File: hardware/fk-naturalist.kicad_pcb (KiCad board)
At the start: 2 copper layers, 106 x 37 mm, 140 parts, among them J1 Conn_01x11, J10 S2B-PH-SM4-TB, J11 RF-SMA-EDGE, J2 Conn_01x05, J3 Conn_01x04, J5 Conn_01x03, J6 Conn_01x05, J7 CONN-HDR-2x5, J8 Conn_01x09, J9 MICRO-USB, M1 MOUNT_HOLE, M3 MOUNT_HOLE, M4 MOUNT_HOLE, M6 MOUNT_HOLE, M7 MICROSD, Q1 2N7002LT1G, Q2 2N7002LT1G, Q3 2N7002LT1G, Q4 2N7002LT1G, SW1 SPNO, SW2 SPNO, U1 ATWINC1500-MR210PA, U10 FGPMMOPA6H, U101 TSL2591, U102 MPL3115A2, U103 BNO055, U104 SHT31, U11 MAX1704XX, U2 ATSAMD21G18A-AU, U3 SPH0645, U4 24AA02E64, U5 S25FL116K0XMFI041, U6 BQ24074RGTT, U7 PCF8523, U8 MCP1700T-3302E/MB, U9 ISL8541x, Y1 FC-135, Y101 FC-135, Y2 FC-135

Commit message: More label/naming cleanup.
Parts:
- C10, C19, C20, C25: value 4.7uF 10V X5R -> 4.7uF
- C12: value 1uF 50V X5R -> 1uF
- C14: value 4.7nF 25V X7R -> 4.7nF
- C21, C23, C27, C29, C6: value 1uF 10V X5R -> 1uF
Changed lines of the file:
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@@
     (links 368)
     (no_connects 106)
-    (area 62.463333 99.838199 191.661515 152.064743)
+    (area 77.293399 109.703799 183.463001 146.887001)
     (thickness 1.6)
     (drawings 52)
@@
   )
   (layers
-    (0 F.Cu signal hide)
+    (0 F.Cu signal)
     (31 B.Cu signal)
     (32 B.Adhes user)
@@
     (46 B.CrtYd user)
     (47 F.CrtYd user)
-    (48 B.Fab user hide)
+    (48 B.Fab user)
     (49 F.Fab user)
   )
@@
       (effects (font (size 1 1) (thickness 0.15)))
     )
-    (fp_text value "1uF 10V X5R" (at 0.5969 0.1016 90) (layer F.Fab)
+    (fp_text value 1uF (at 0.5969 0.1016 90) (layer F.Fab)
       (effects (font (size 1 1) (thickness 0.15)))
     )
@@
       (effects (font (size 1 1) (thickness 0.15)))
     )
-    (fp_text value "4.7uF 10V X5R" (at 0.198714 0.095444) (layer F.Fab)
+    (fp_text value 4.7uF (at -3.369986 0.082744) (layer F.Fab)
       (effects (font (size 1 1) (thickness 0.15)))
     )
@@
       (effects (font (size 1 1) (thickness 0.15)))
     )
-    (fp_text value "1uF 50V X5R" (at -1.652953 -0.050941 180) (layer F.Fab)
+    (fp_text value 1uF (at -0.103553 1.384159 180) (layer F.Fab)
       (effects (font (size 1 1) (thickness 0.15)))
     )
@@
       (effects (font (size 1 1) (thickness 0.15)))
     )
-    (fp_text value "4.7nF 25V X7R" (at 7.235195 0.175542 90) (layer F.Fab)
+    (fp_text value 4.7nF (at 0.135895 1.534442 90) (layer F.Fab)
       (effects (font (size 1 1) (thickness 0.15)))
     )
@@
       (effects (font (size 1 1) (thickness 0.15)))
     )
-    (fp_text value "4.7uF 10V X5R" (at -2.4892 1.4478 180) (layer F.Fab)
+    (fp_text value 4.7uF (at -0.2159 1.4605 180) (layer F.Fab)
       (effects (font (size 1 1) (thickness 0.15)))
     )
@@
       (effects (font (size 1 1) (thickness 0.15)))
     )
-    (fp_text value "4.7uF 10V X5R" (at 2.085653 0.241441) (layer F.Fab)
+    (fp_text value 4.7uF (at -2.054547 0.038241) (layer F.Fab)
       (effects (font (size 1 1) (thickness 0.15)))
     )
@@
       (effects (font (size 1 1) (thickness 0.15)))
     )
-    (fp_text value "1uF 10V X5R" (at 0.713153 0.012841) (layer F.Fab)
+    (fp_text value 1uF (at -2.601547 -0.025259) (layer F.Fab)
       (effects (font (size 1 1) (thickness 0.15)))
     )
@@
       (effects (font (size 1 1) (thickness 0.15)))
     )
-    (fp_text value "4.7uF 10V X5R" (at -1.581277 -0.0254 270) (layer F.Fab)
+    (fp_text value 4.7uF (at 2.622423 -0.0635 270) (layer F.Fab)
       (effects (font (size 1 1) (thickness 0.15)))
     )
@@
       (effects (font (size 1 1) (thickness 0.15)))
     )
-    (fp_text value 100nF (at 3.371723 0.047919 270) (layer F.Fab)
+    (fp_text value 100nF (at 3.066923 -0.015581 270) (layer F.Fab)
       (effects (font (size 1 1) (thickness 0.15)))
     )
@@
       (effects (font (size 1 1) (thickness 0.15)))
     )
-    (fp_text value "1uF 10V X5R" (at 6.43231 0.026186) (layer F.Fab)
+    (fp_text value 1uF (at 2.83821 0.013486) (layer F.Fab)
       (effects (font (size 1 1) (thickness 0.15)))
     )
@@
       (effects (font (size 1 1) (thickness 0.15)))
     )
-    (fp_text value 10nF (at -3.21921 0.062714 180) (layer F.Fab)
+    (fp_text value 10nF (at -2.27941 0.989814 180) (layer F.Fab)
       (effects (font (size 1 1) (thickness 0.15)))
     )
@@
       (effects (font (size 1 1) (thickness 0.15)))
     )
-    (fp_text value "1uF 10V X5R" (at -3.5297 1.3589 270) (layer F.Fab)
+    (fp_text value 1uF (at -0.4563 1.3843 270) (layer F.Fab)
       (effects (font (size 1 1) (thickness 0.15)))
     )
@@
       (effects (font (size 1 1) (thickness 0.15)))
     )
-    (fp_text value 100pF (at 0 1.9 90) (layer F.Fab)
+    (fp_text value 100pF (at -0.889644 -1.312786 90) (layer F.Fab)
       (effects (font (size 1 1) (thickness 0.15)))
     )
@@
       (effects (font (size 1 1) (thickness 0.15)))
     )
-    (fp_text value Green (at -3.8862 1.1938 180) (layer F.Fab)
+    (fp_text value Green (at -0.1524 1.4732 180) (layer F.Fab)
       (effects (font (size 1 1) (thickness 0.15)))
     )
@@
       (effects (font (size 1 1) (thickness 0.15)))
     )
-    (fp_text value 24AA02E64 (at 6.584592 -0.101358 90) (layer F.Fab)
+    (fp_text value 24AA02E64 (at 6.038492 -0.126758 90) (layer F.Fab) hide
       (effects (font (size 1 1) (thickness 0.15)))
     )
-    (fp_text user %R (at 0 0 180) (layer F.Fab)
+    (fp_text user %R (at 0 0 180) (layer F.Fab) hide
       (effects (font (size 0.5 0.5) (thickness 0.075)))
     )
@@
       (effects (font (size 1 1) (thickness 0.15)))
     )
-    (fp_text value 1uF (at -2.569376 0.0889 90) (layer F.Fab)
+    (fp_text value 1uF (at 2.777324 -0.0127 90) (layer F.Fab)
       (effects (font (size 1 1) (thickness 0.15)))
     )
@@
       (effects (font (size 1 1) (thickness 0.15)))
     )
-    (fp_text value "1uF 10V X5R" (at -0.5461 0 180) (layer F.Fab)
+    (fp_text value 1uF (at -0.5461 0 180) (layer F.Fab)
       (effects (font (size 1 1) (thickness 0.15)))
     )

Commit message: Fix USB footprint with oval drills.
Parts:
- J9: footprint RocketScreamKicadLibrary:MICRO-USB -> conservify:MICRO-USB
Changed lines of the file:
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@@
   (general
     (links 368)
-    (no_connects 106)
+    (no_connects 0)
     (area 77.293399 109.703799 183.463001 146.887001)
     (thickness 1.6)
@@
       (net 2 3V3))
   )
-  (module RocketScreamKicadLibrary:MICRO-USB (layer F.Cu)
-    (at 80.9752 122.8344 270)
-    (tags MICRO-USB)
-    (fp_text reference J9 (at 0 -3.556 270) (layer F.SilkS) hide
-      (effects (font (size 1 1) (thickness 0.15)))
-    )
-    (fp_text value MICRO-USB (at 0 4.318 270) (layer F.Fab) hide
-      (effects (font (size 1 1) (thickness 0.15)))
-    )
-    (fp_line (start -4.55 -2.4) (end -4.55 3.45) (layer F.CrtYd) (width 0.05))
-    (fp_line (start -4.55 3.45) (end 4.55 3.45) (layer F.CrtYd) (width 0.05))
-    (fp_line (start 4.55 3.45) (end 4.55 -2.4) (layer F.CrtYd) (width 0.05))
-    (fp_line (start 4.55 -2.4) (end -4.55 -2.4) (layer F.CrtYd) (width 0.05))
-    (fp_circle (center -1.746 -2.608) (end -1.796 -2.658) (layer F.SilkS) (width 0.3))
-    (fp_line (start 3.8 0) (end 3.8 -1.55) (layer F.SilkS) (width 0.15))
-    (fp_line (start 3.8 -1.55) (end 3.25 -1.55) (layer F.SilkS) (width 0.15))
-    (fp_line (start -3.8 0) (end -3.8 -1.55) (layer F.SilkS) (width 0.15))
-    (fp_line (start -3.8 -1.55) (end -3.25 -1.55) (layer F.SilkS) (width 0.15))
-    (fp_line (start 3.8 2.2) (end 3.8 3.3) (layer F.SilkS) (width 0.15))
-    (fp_line (start -3.8 3.3) (end -3.8 2.2) (layer F.SilkS) (width 0.15))
-    (fp_line (start -3.8 3.3) (end 3.8 3.3) (layer F.SilkS) (width 0.15))
-    (pad 1 smd rect (at -1.3 -1.45 270) (size 0.4 1.35) (layers F.Cu F.Paste F.Mask)
-      (net 44 VUSB))
-    (pad 2 smd rect (at -0.65 -1.45 270) (size 0.4 1.35) (layers F.Cu F.Paste F.Mask)
-      (net 22 /USB-))
-    (pad 3 smd rect (at 0 -1.45 270) (size 0.4 1.35) (layers F.Cu F.Paste F.Mask)
-      (net 23 /USB+))
-    (pad 4 smd rect (at 0.65 -1.45 270) (size 0.4 1.35) (layers F.Cu F.Paste F.Mask)
-      (net 80 "Net-(J9-Pad4)"))
-    (pad 5 smd rect (at 1.3 -1.45 270) (size 0.4 1.35) (layers F.Cu F.Paste F.Mask)
-      (net 1 GND))
-    (pad 6 thru_hole circle (at -2.425 -1.525 270) (size 1.2 1.2) (drill 0.7) (layers *.Cu *.Mask F.SilkS)
-      (net 56 "Net-(C14-Pad1)"))
-    (pad 7 thru_hole circle (at 2.425 -1.525 270) (size 1.2 1.2) (drill 0.7) (layers *.Cu *.Mask F.SilkS)
-      (net 143 "Net-(J9-Pad7)"))
-    (pad 8 thru_hole oval (at -3.625 1.125 270) (size 1.3 1.7) (drill oval 0.7 1.1) (layers *.Cu *.Mask F.SilkS)
-      (net 81 "Net-(J9-Pad8)"))
-    (pad 9 thru_hole oval (at 3.625 1.125 270) (size 1.3 1.7) (drill oval 0.7 1.1) (layers *.Cu *.Mask F.SilkS)
-      (net 82 "Net-(J9-Pad9)"))
-  )
   (module RocketScreamKicadLibrary:S2B-PH-SM4-TB (layer F.Cu)
     (at 85.2452 141.726)
@@
     )
   )
+  (module conservify:MICRO-USB (layer F.Cu)
+    (at 80.9752 122.8344 270)
+    (tags MICRO-USB)
+    (fp_text reference J9 (at -26.162 0 270) (layer F.SilkS) hide
+      (effects (font (size 0.8 0.8) (thickness 0.15)))
+    )
+    (fp_text value MICRO-USB (at 0 4.318 270) (layer F.Fab) hide
+      (effects (font (size 0.8 0.8) (thickness 0.15)))
+    )
+    (fp_line (start -4.55 -2.4) (end -4.55 3.45) (layer F.CrtYd) (width 0.05))
+    (fp_line (start -4.55 3.45) (end 4.55 3.45) (layer F.CrtYd) (width 0.05))
+    (fp_line (start 4.55 3.45) (end 4.55 -2.4) (layer F.CrtYd) (width 0.05))
+    (fp_line (start 4.55 -2.4) (end -4.55 -2.4) (layer F.CrtYd) (width 0.05))
+    (fp_circle (center -1.746 -2.608) (end -1.796 -2.658) (layer F.SilkS) (width 0.3))
+    (fp_line (start 3.8 0) (end 3.8 -1.55) (layer F.SilkS) (width 0.15))
+    (fp_line (start 3.8 -1.55) (end 3.25 -1.55) (layer F.SilkS) (width 0.15))
+    (fp_line (start -3.8 0) (end -3.8 -1.55) (layer F.SilkS) (width 0.15))
+    (fp_line (start -3.8 -1.55) (end -3.25 -1.55) (layer F.SilkS) (width 0.15))
+    (fp_line (start 3.8 2.2) (end 3.8 3.3) (layer F.SilkS) (width 0.15))
+    (fp_line (start -3.8 3.3) (end -3.8 2.2) (layer F.SilkS) (width 0.15))
+    (fp_line (start -3.8 3.3) (end 3.8 3.3) (layer F.SilkS) (width 0.15))
+    (pad 1 smd rect (at -1.3 -1.45 270) (size 0.4 1.35) (layers F.Cu F.Paste F.Mask)
+      (net 44 VUSB))
+    (pad 2 smd rect (at -0.65 -1.45 270) (size 0.4 1.35) (layers F.Cu F.Paste F.Mask)
+      (net 22 /USB-))
+    (pad 3 smd rect (at 0 -1.45 270) (size 0.4 1.35) (layers F.Cu F.Paste F.Mask)
+      (net 23 /USB+))
+    (pad 4 smd rect (at 0.65 -1.45 270) (size 0.4 1.35) (layers F.Cu F.Paste F.Mask)
+      (net 80 "Net-(J9-Pad4)"))
+    (pad 5 smd rect (at 1.3 -1.45 270) (size 0.4 1.35) (layers F.Cu F.Paste F.Mask)
+      (net 1 GND))
+    (pad 6 thru_hole circle (at -2.425 -1.525 270) (size 1.2 1.2) (drill 0.7) (layers *.Cu *.Mask F.Paste)
+      (net 56 "Net-(C14-Pad1)"))
+    (pad 7 thru_hole circle (at 2.425 -1.525 270) (size 1.2 1.2) (drill 0.7) (layers *.Cu *.Mask F.Paste)
+      (net 143 "Net-(J9-Pad7)"))
+    (pad 8 thru_hole circle (at -3.625 1.125 270) (size 1.7 1.7) (drill oval 1.1) (layers *.Cu *.Mask F.Paste)
+      (net 81 "Net-(J9-Pad8)"))
+    (pad 9 thru_hole circle (at 3.625 1.125 270) (size 1.7 1.7) (drill oval 1.1) (layers *.Cu *.Mask F.Paste)
+      (net 82 "Net-(J9-Pad9)"))
+  )
   (gr_text DATA (at 94.8817 141.1351 270) (layer F.SilkS)

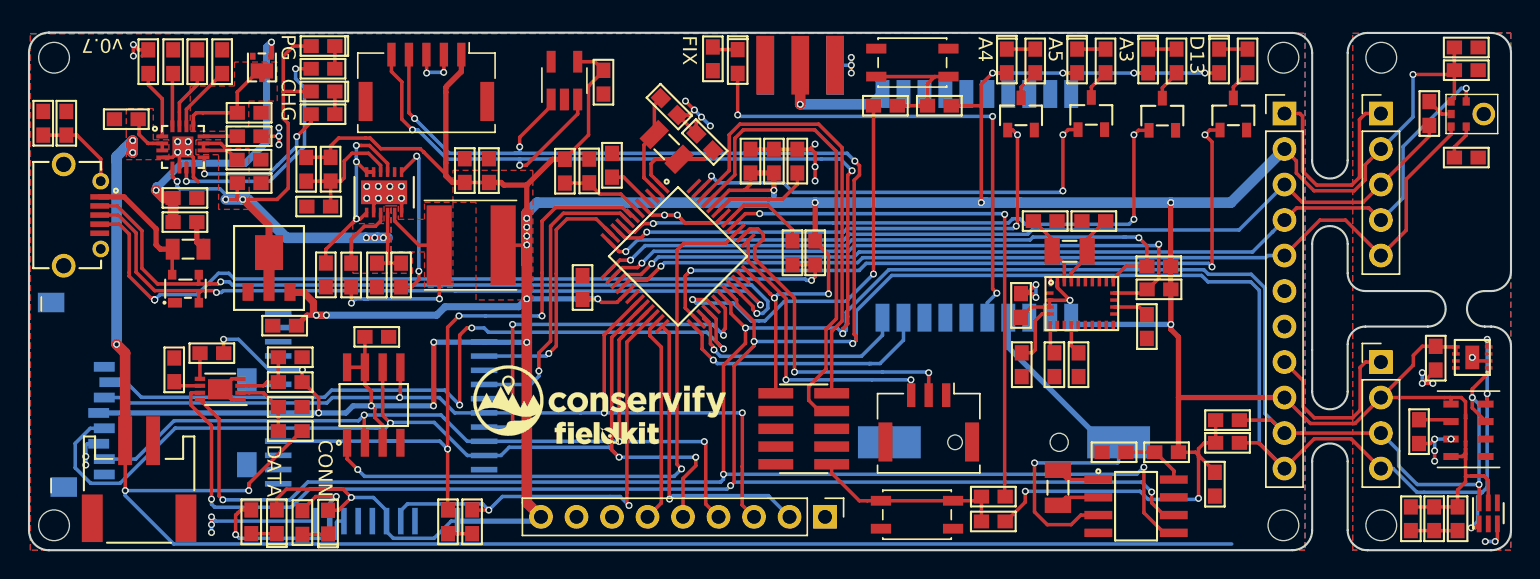
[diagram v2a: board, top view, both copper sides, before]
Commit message: Moving some parts in from the edge.
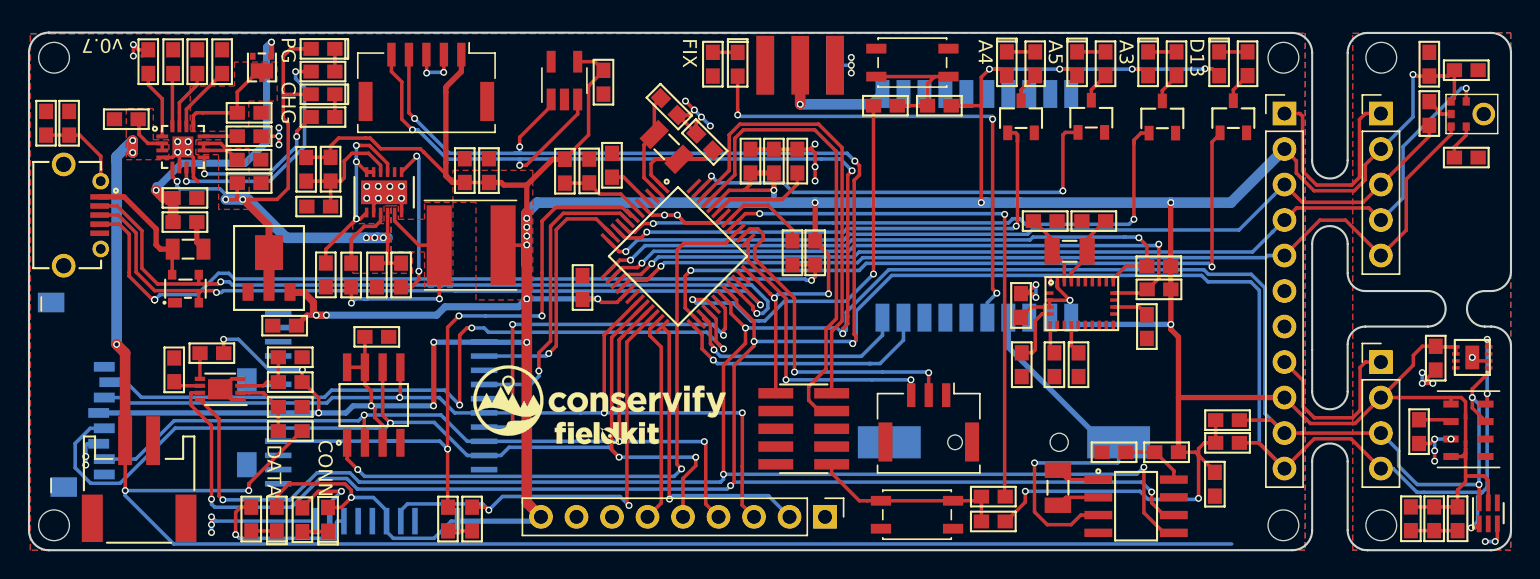
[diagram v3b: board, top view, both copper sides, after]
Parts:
- moved C15 2.90 mm to (177.5, 112.0), turned to 90 degrees
- moved R39 0.38 mm to (126.3, 112.0)
- moved R5 0.20 mm to (96.9, 144.6)
- moved C14 0.20 mm to (80.2, 116.3)
- moved D1 0.20 mm to (162.5, 112.0)
- moved D10 0.20 mm to (98.4, 114.2)
- moved D11 0.20 mm to (128.1, 112.0)
- moved D4 0.20 mm to (157.4, 112.0)
- moved D5 0.20 mm to (147.3, 112.0)
- moved D6 0.20 mm to (152.3, 112.0)
- moved D9 0.20 mm to (98.4, 110.9)
- moved Q1 0.20 mm to (163.5, 115.8)
- moved Q2 0.20 mm to (158.4, 115.8)
- moved Q3 0.20 mm to (148.3, 115.8)
- moved Q4 0.20 mm to (153.4, 115.8)
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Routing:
- net 3V3: track 436.5 -> 437.7 mm
- net /D13: track 52.7 -> 51.7 mm, vias 3 -> 2
- net Net-(R5-Pad1): track 4.83 -> 5.84 mm
- net /SDA: track 236.6 -> 237.6 mm
- net /SCL: track 242.3 -> 242.9 mm
- net /A4: track 36.5 -> 36.9 mm, vias 3 -> 2
- net /A3: track 44.7 -> 44.4 mm, vias 3 -> 2
- net /A5: track 32.4 -> 32.3 mm, vias 3 -> 2
